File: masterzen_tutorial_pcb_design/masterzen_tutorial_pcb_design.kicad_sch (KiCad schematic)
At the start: 27 parts, among them SW85 SW_SPDT, U1 AMS1117, U3 PRTR5V0U2X, U4 STM32F303RETx, Y1 16MHz

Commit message: replaced polyfuse with ferrite bead
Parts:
- removed F1: Polyfuse_Small, symbol Device:Polyfuse_Small
- added FB2: FerriteBead, symbol Device:FerriteBead
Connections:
- net VBUS: now also FB2.2
- net at USB1.11 (VBUS), USB1.2 (VBUS): now also FB2.1
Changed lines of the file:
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@@
 	)
 	(junction
-		(at 57.15 93.98)
-		(diameter 0)
-		(color 0 0 0 0)
-	)
-	(junction
 		(at 102.87 109.22)
 		(diameter 0)
@@
 	)
 	(junction
+		(at 57.15 93.98)
+		(diameter 0)
+		(color 0 0 0 0)
+	)
+	(junction
 		(at 167.64 106.68)
 		(diameter 0)
@@
 	(wire
 		(pts
-			(xy 57.15 93.98) (xy 68.58 93.98)
-		)
-		(stroke
-			(width 0)
-			(type default)
-		)
-	)
-	(wire
-		(pts
 			(xy 170.18 93.98) (xy 165.1 93.98)
 		)
@@
 	(wire
 		(pts
-			(xy 73.66 93.98) (xy 81.28 93.98)
-		)
-		(stroke
-			(width 0)
-			(type default)
-		)
-	)
-	(wire
-		(pts
 			(xy 35.56 63.5) (xy 35.56 66.04)
 		)
@@
 	(wire
 		(pts
+			(xy 74.93 93.98) (xy 81.28 93.98)
+		)
+		(stroke
+			(width 0)
+			(type default)
+		)
+	)
+	(wire
+		(pts
 			(xy 77.47 106.68) (xy 110.49 106.68)
 		)
@@
 	(wire
 		(pts
+			(xy 57.15 93.98) (xy 67.31 93.98)
+		)
+		(stroke
+			(width 0)
+			(type default)
+		)
+	)
+	(wire
+		(pts
 			(xy 241.3 52.07) (xy 247.65 52.07)
 		)
@@
 	)
 	(symbol
-		(lib_id "Device:Polyfuse_Small")
+		(lib_id "Device:FerriteBead")
 		(at 71.12 93.98 90)
 		(unit 1)
@@
 		(dnp no)
 		(fields_autoplaced yes)
-		(property "Reference" "F1"
-			(at 71.12 87.63 90)
+		(property "Reference" "FB2"
+			(at 71.0692 86.36 90)
 			(effects
 				(font
@@
 			)
 		)
-		(property "Value" "Polyfuse_Small"
-			(at 71.12 90.17 90)
+		(property "Value" "FerriteBead"
+			(at 71.0692 88.9 90)
 			(effects
 				(font
@@
 		)
 		(property "Footprint" ""
-			(at 76.2 92.71 0)
+			(at 71.12 95.758 90)
 			(effects
 				(font
 					(size 1.27 1.27)
 				)
-				(justify left)
 				(hide yes)
 			)
@@
 			)
 		)
-		(property "Description" "Resettable fuse, polymeric positive temperature coefficient, small symbol"
+		(property "Description" "Ferrite bead"
 			(at 71.12 93.98 0)
 			(effects
@@
 			)
 		)
-		(pin "1"
-		)
 		(pin "2"
 		)
+		(pin "1"
+		)
 		(instances
-			(project "masterzen_tutorial_pcb_design"
+			(project ""
 				(path "/43ab7f41-8dc3-471f-b30f-d5100c2539fd"
-					(reference "F1")
+					(reference "FB2")
 					(unit 1)
 				)

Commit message: finished schematic
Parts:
- removed FB2: FerriteBead, symbol Device:FerriteBead
- removed R1: 10k, symbol Device:R
- removed SW85: SW_SPDT, symbol Switch:SW_SPDT
- added D16: Caps Lock LED, symbol Device:LED
- added F1: Polyfuse_Small, Fuse:Fuse_0805_2012Metric_Pad1.15x1.40mm_HandSolder, symbol Device:Polyfuse_Small
- added R2, R8, R9: 5.1k, symbol Device:R
- added R6, R7: 5.1k, Resistor_SMD:R_0805_2012Metric_Pad1.20x1.40mm_HandSolder, symbol Device:R
- added SW1: SW_Push, Button_Switch_SMD:SW_SPST_SKQG_WithStem, symbol Switch:SW_Push
- added SW2: RotaryEncoder_Switch, Rotary_Encoder:RotaryEncoder_Alps_EC11E-Switch_Vertical_H20mm_CircularMountingHoles, symbol Device:RotaryEncoder_Switch
- C1: renamed from C12; value C_Small -> 22uF; footprint (none) -> Capacitor_SMD:C_0805_2012Metric_Pad1.18x1.45mm_HandSolder
- C10, C11: footprint (none) -> Capacitor_SMD:C_0805_2012Metric_Pad1.18x1.45mm_HandSolder
- C12: renamed from C3; footprint (none) -> Capacitor_SMD:C_0805_2012Metric_Pad1.18x1.45mm_HandSolder
- C13: renamed from C2; footprint (none) -> Capacitor_SMD:C_0805_2012Metric_Pad1.18x1.45mm_HandSolder
- C2: renamed from C13; value C_Small -> 22uF; footprint (none) -> Capacitor_SMD:C_0805_2012Metric_Pad1.18x1.45mm_HandSolder
- C3: renamed from C5; footprint (none) -> Capacitor_SMD:C_0805_2012Metric_Pad1.18x1.45mm_HandSolder
- C4: renamed from C6; footprint (none) -> Capacitor_SMD:C_0805_2012Metric_Pad1.18x1.45mm_HandSolder
- C5: renamed from C7; footprint (none) -> Capacitor_SMD:C_0805_2012Metric_Pad1.18x1.45mm_HandSolder
- C6: renamed from C8; footprint (none) -> Capacitor_SMD:C_0805_2012Metric_Pad1.18x1.45mm_HandSolder
- C7: renamed from C9; footprint (none) -> Capacitor_SMD:C_0805_2012Metric_Pad1.18x1.45mm_HandSolder
- C8: renamed from C4; footprint (none) -> Capacitor_SMD:C_0805_2012Metric_Pad1.18x1.45mm_HandSolder
- C9: renamed from C1; footprint (none) -> Capacitor_SMD:C_0805_2012Metric_Pad1.18x1.45mm_HandSolder
- D1: renamed from D85; footprint (none) -> LED_SMD:LED_0201_0603Metric_Pad0.64x0.40mm_HandSolder
- FB1: footprint (none) -> Ferrite_THT:LairdTech_28C0236-0JW-10
- R1: renamed from R3; value R -> 1.5k; footprint (none) -> Resistor_SMD:R_0805_2012Metric_Pad1.20x1.40mm_HandSolder
- R3: renamed from R6; footprint (none) -> Resistor_SMD:R_0805_2012Metric_Pad1.20x1.40mm_HandSolder
- R4: renamed from R2; footprint (none) -> Resistor_SMD:R_0805_2012Metric_Pad1.20x1.40mm_HandSolder
- R5: footprint (none) -> Resistor_SMD:R_0805_2012Metric_Pad1.20x1.40mm_HandSolder
- U2: renamed from U3; footprint (none) -> random-keyboard-parts:SOT143B
- USB1: footprint (none) -> Type-C:HRO-TYPE-C-31-M-12-HandSoldering
- Y1: footprint (none) -> Crystal:Crystal_SMD_3225-4Pin_3.2x2.5mm
- renumbered U4 to U3
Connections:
- net VCC is gone; now on net +3.3V: U2.4 (VCC)
- net +3.3V: now also R6.2, R7.2, SW1.1
- net GND: now also R8.2, R9.1, SW2.C
- net VBUS: now also F1.2
- net at U3.4 (PC15): now also D16.2 (A)
- net BOOT0: now reaches U3.60 (BOOT0)
- net BOOT0: now also R2.1, SW1.2
- net at USB1.11 (VBUS), USB1.2 (VBUS): now also F1.1
- new net: R6.1, SW2.B
- new net: D16.1 (K), R8.1
- new net: R2.2, R9.2
- new net: R7.1, SW2.A
- new net ROT_ENC_COL: SW2.S1
- new net ROT_ENC_ROW: SW2.S2
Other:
- note removed: "USB C"
- moved on the sheet: C1, C10, C11, C12, C13, C2, C3, C4, C5, C6, C7, C8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

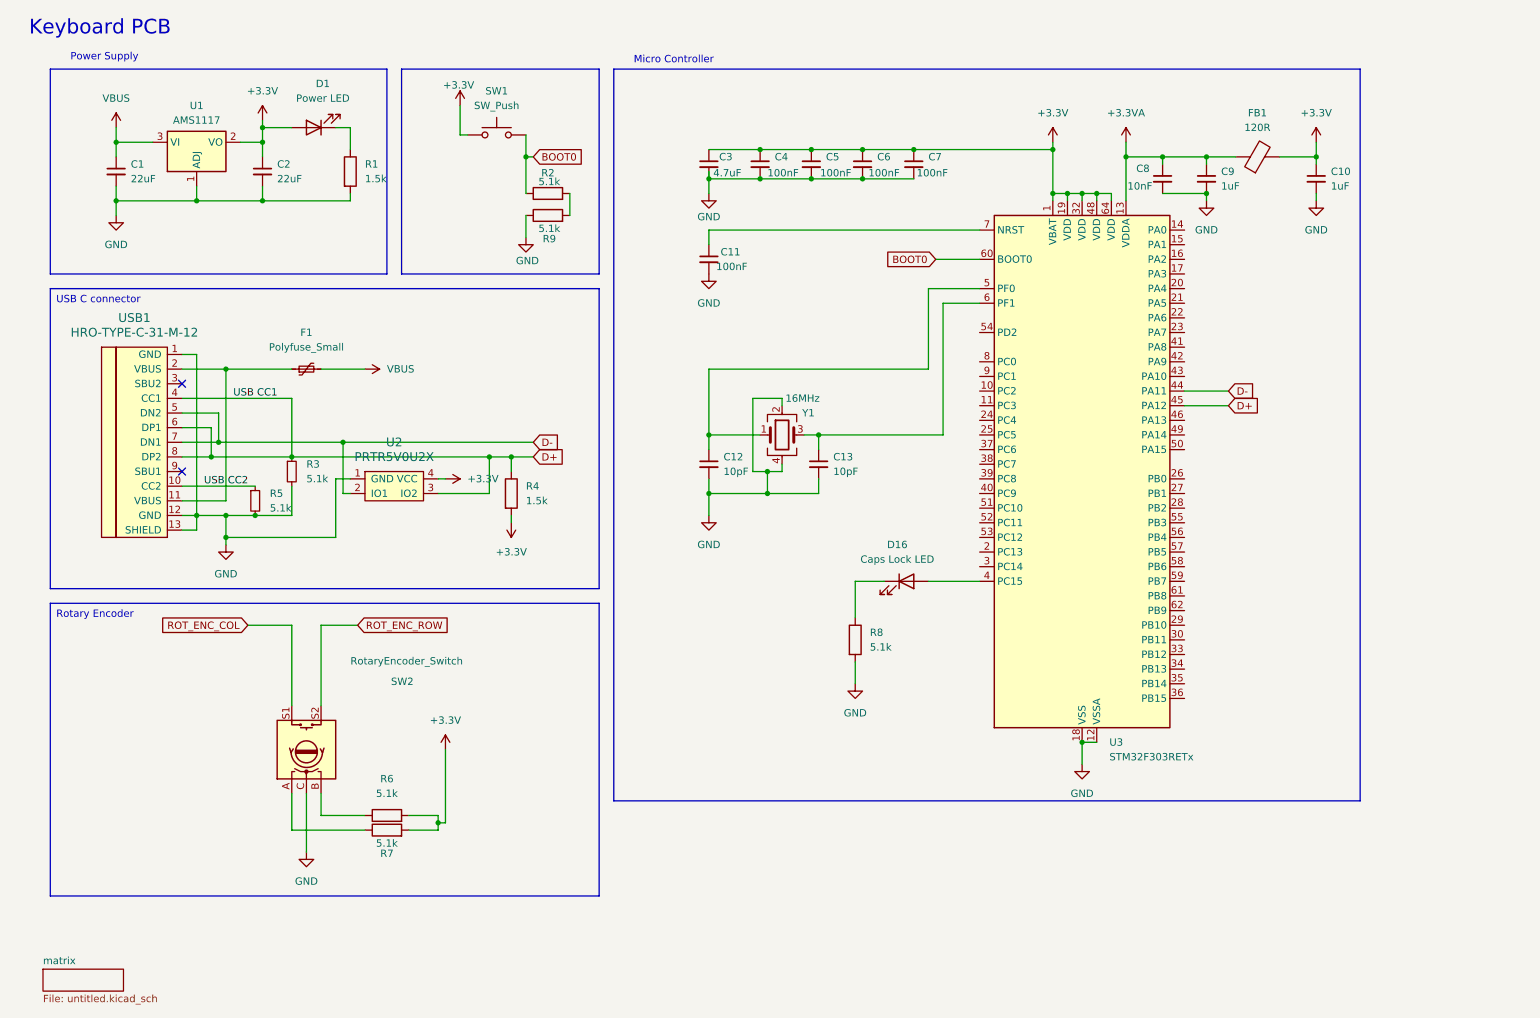
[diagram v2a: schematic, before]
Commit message: starting placing components on a pcb
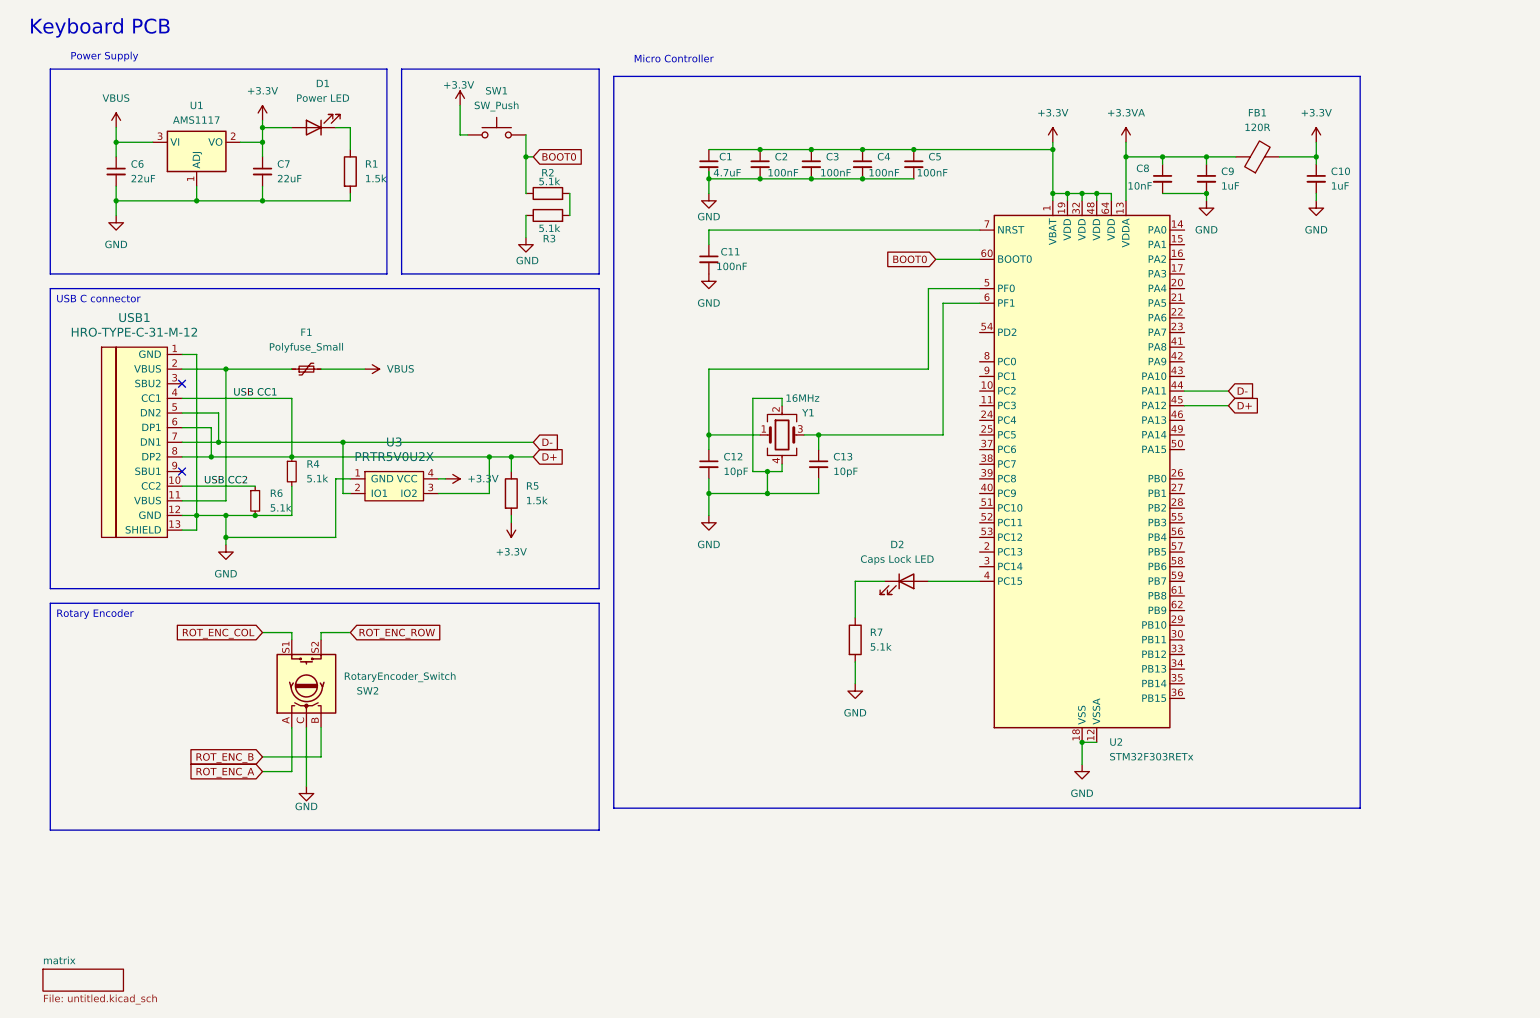
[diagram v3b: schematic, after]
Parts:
- removed R6, R7: 5.1k, Resistor_SMD:R_0805_2012Metric_Pad1.20x1.40mm_HandSolder, symbol Device:R
- D2: renamed from D16; footprint (none) -> LED_SMD:LED_0805_2012Metric_Pad1.15x1.40mm_HandSolder
- R2: footprint (none) -> Resistor_SMD:R_0805_2012Metric_Pad1.20x1.40mm_HandSolder
- R3: renamed from R9; footprint (none) -> Resistor_SMD:R_0805_2012Metric_Pad1.20x1.40mm_HandSolder
- R7: renamed from R8; footprint (none) -> Resistor_SMD:R_0805_2012Metric_Pad1.20x1.40mm_HandSolder
- renumbered C3 to C1, C4 to C2, C5 to C3, C6 to C4, C7 to C5, C1 to C6, C2 to C7, R3 to R4, R4 to R5, R5 to R6, U3 to U2, U2 to U3
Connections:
- net ROT_ENC_B: now reaches SW2.B
- net ROT_ENC_A: now reaches SW2.A
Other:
- moved on the sheet: SW2

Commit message: updated
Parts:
- F1: footprint Fuse:Fuse_0805_2012Metric_Pad1.15x1.40mm_HandSolder -> Inductor_SMD:L_0603_1608Metric
- FB1: footprint Ferrite_THT:LairdTech_28C0236-0JW-10 -> Inductor_SMD:L_0603_1608Metric
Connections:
- net D+: no longer R4.1, USB1.4 (CC1)
- net XTAL_IN: now reaches C12.1, U2.5 (PF0), Y1.1
- net XTAL_OUT: now reaches C13.1, U2.6 (PF1), Y1.3
- net PC15: now reaches D2.2 (A), U2.4 (PC15)
- new net USB CC1: R4.1, USB1.4 (CC1)
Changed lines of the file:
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@@
 	)
 	(junction
-		(at 67.31 92.71)
-		(diameter 0)
-		(color 0 0 0 0)
-	)
-	(junction
 		(at 207.01 46.99)
 		(diameter 0)
@@
 	(wire
 		(pts
-			(xy 67.31 92.71) (xy 101.6 92.71)
-		)
-		(stroke
-			(width 0)
-			(type default)
-		)
-	)
-	(wire
-		(pts
 			(xy 62.23 38.1) (xy 62.23 40.64)
 		)
@@
 	(wire
 		(pts
-			(xy 53.34 92.71) (xy 67.31 92.71)
+			(xy 53.34 92.71) (xy 101.6 92.71)
 		)
 		(stroke
@@
 	)
 	(rectangle
-		(start 123.19 26.67)
-		(end 252.73 153.67)
+		(start 123.19 25.4)
+		(end 252.73 157.48)
 		(stroke
 			(width 0)
@@
 		)
 	)
+	(global_label "XTAL_IN"
+		(shape input)
+		(at 156.21 77.47 90)
+		(fields_autoplaced yes)
+		(effects
+			(font
+				(size 1.27 1.27)
+			)
+			(justify left)
+		)
+		(property "Intersheetrefs" "${INTERSHEET_REFS}"
+			(at 156.21 67.2881 90)
+			(effects
+				(font
+					(size 1.27 1.27)
+				)
+				(justify left)
+				(hide yes)
+			)
+		)
+	)
+	(global_label "XTAL_OUT"
+		(shape input)
+		(at 170.18 88.9 270)
+		(fields_autoplaced yes)
+		(effects
+			(font
+				(size 1.27 1.27)
+			)
+			(justify right)
+		)
+		(property "Intersheetrefs" "${INTERSHEET_REFS}"
+			(at 170.18 100.7752 90)
+			(effects
+				(font
+					(size 1.27 1.27)
+				)
+				(justify right)
+				(hide yes)
+			)
+		)
+	)
+	(global_label "PC15"
+		(shape input)
+		(at 182.88 114.3 270)
+		(fields_autoplaced yes)
+		(effects
+			(font
+				(size 1.27 1.27)
+			)
+			(justify right)
+		)
+		(property "Intersheetrefs" "${INTERSHEET_REFS}"
+			(at 182.88 122.2442 90)
+			(effects
+				(font
+					(size 1.27 1.27)
+				)
+				(justify right)
+				(hide yes)
+			)
+		)
+	)
 	(global_label "ROT_ENC_COL"
 		(shape input)
@@
 			)
 		)
-		(property "Footprint" "Ferrite_THT:LairdTech_28C0236-0JW-10"
+		(property "Footprint" "Inductor_SMD:L_0603_1608Metric"
 			(at 234.95 42.418 90)
 			(effects
@@
 			)
 		)
-		(property "Footprint" "Fuse:Fuse_0805_2012Metric_Pad1.15x1.40mm_HandSolder"
+		(property "Footprint" "Inductor_SMD:L_0603_1608Metric"
 			(at 74.93 76.2 0)
 			(effects
